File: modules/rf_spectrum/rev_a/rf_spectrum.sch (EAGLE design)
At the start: 43 parts, among them J1 MODULE_GENERIC, J7 TC2030-JLINK-L, P1 MOLEX_73251-135X, P2 MOLEX_73251-135X, P3 MOLEX_73251-135X, U1 SAM4LC8AA, U2 MWSUB3G, U3 SKY13317, U7 TLV62130, X1 16MHz

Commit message: schematic done, much routing done
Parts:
- removed C1, C2: 8pF, passives:CAPACITOR0603_CAP
- removed C16, C17, C18, C19: 100nF, passives:CAPACITOR0603_CAP
- removed C20: 100nF, passives:CAPACITOR0402_CAP
- removed C24: 4.7uF, passives:CAPACITOR0402_CAP
- removed FB1: 1.5kΩ, passives:FERRITE_BEAD0603
- removed L2: 22uH, signpost:LHQ3NP
- removed R15, R16: 100k, passives:RESISTOR0603_RES
- removed R25: 0, passives:RESISTOR0603_RES
- removed R7: 10k, passives:RESISTOR0603_RES
- removed TP11, TP12, TP13, TP14, TP15, TP16: TEST_POINT_0.040IN, headers:TEST_POINT_0.040IN
- removed X1: 16MHz, crystals:FH1600015
- added C11: 10nF, passives:CAPACITOR0402_CAP
- added C12: 1uF, passives:CAPACITOR0402_CAP
- added C13, C14: 4.3pF, passives:CAPACITOR0402_CAP
- added C7: 4.7uF, passives:CAPACITOR0402_CAP
- added C8, C9: 100nF, passives:CAPACITOR0402_CAP
- added D1: GREEN, leds:LED0603
- added D2: RED, leds:LED0603
- added R1, R3, R4: 10k, passives:RESISTOR0402_RES
- added R2: 100k, passives:RESISTOR0402_RES
- added X2: ABS05-32.768KHZ-9-T, crystals:ABS05-32.768KHZ-9-T
- C3, C4, C5, C6: device passives:CAPACITOR0603_CAP -> passives:CAPACITOR0402_CAP
- J1: value MODULE_GENERIC -> MODULE_GENERIC_DEBUGSMT; device signpost:MODULE_GENERIC -> signpost:MODULE_GENERIC_DEBUGSMT
- U1: value SAM4LC8AA -> STM32L432KC; device chips:SAM4LC8AA -> chips:STM32L432KC
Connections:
- removed net !CONTROLLER_RESET: J7.!RESET, S1.P$2, U1.!RESET
- removed net CONTROLLER_BUCK/LDO_N: R25.2, R7.1, U1.PA02
- removed net CONTROLLER_SWDCLK: J7.SWDCLK, R16.1, U1.TCK
- removed net CONTROLLER_SWDIO: J7.SWDIO, R15.1, U1.PA03
- removed net CONTROLLER_XIN: C1.1, U1.PA00, X1.2
- removed net CONTROLLER_XOUT: C2.1, U1.PA01, X1.1
- removed net N$32: C16.1, FB1.P$1, U1.VDDANA
- removed net N$44: C20.1, C24.1, L2.1, U1.VDDOUT
- removed net N$52: L2.2, U1.VDDCORE
- removed net N$53: U1.BIASH, U1.BIASL
- removed net N$54: U1.CAPH, U1.CAPL
- new net !RST: J1.DBG_!RESET, J7.!RESET, S1.P$2, U1.!RST
- new net DBG_GPIO1: J1.DBG_GPIO1, R3.2, U1.PB0
- new net DBG_GPIO2: J1.DBG_GPIO2, R4.2, U1.PB1
- new net DBG_RX: J1.DBG_RX, U1.PA3
- new net DBG_TX: J1.DBG_TX, U1.PA2
- new net N$10: C13.1, U1.PC15/OSC32OUT, X2.2
- new net N$11: R1.2, U1.PH3/BOOT0
- new net N$12: D1.ANODE, R3.1
- new net N$13: D2.ANODE, R4.1
- new net N$9: C14.1, U1.PC14/OSC32IN, X2.1
- new net SWDCLK: J1.DBG_SWDCLK, J7.SWDCLK, U1.PA14/SWCLK
- new net SWDIO: J1.DBG_SWDIO, J7.SWDIO, U1.PA13/SWDIO
- net 3V3: now also C11.1, C12.1, C7.1, C8.1, C9.1, R2.2, U1.VDD, U1.VDDA/VREF; no longer C17.1, C18.1, C19.1, FB1.P$2, R15.2, R16.2, R7.2, U1.VDDIN, U1.VDDIO, U1.VLCD, U1.VLCDIN
- net GND: now also C11.2, C12.2, C13.2, C14.2, C7.2, C8.2, C9.2, D1.CATHODE, D2.CATHODE, R1.1, U1.VSS; no longer C1.2, C16.2, C17.2, C18.2, C19.2, C2.2, C20.2, C24.2, R25.1, TP11.TESTPOINT, U1.GND, U1.GNDANA, X1.GND
- net MOD_IN: now also U1.PB5; no longer TP14.TESTPOINT, U1.PA20
- net MOD_OUT: now also U1.PB3/JTDO/SWO; no longer TP15.TESTPOINT, U1.PA19
- net PPS: now also U1.PA0/CLKIN; no longer TP16.TESTPOINT, U1.PA18
- net RF_ANT1: now also U1.PA4; no longer U1.PA09
- net RF_ANT2: now also U1.PA5; no longer U1.PA10
- net RF_ANT3: now also U1.PA6; no longer U1.PA11
- net RF_GPIO2: now also U1.PA15/JTDI; no longer U1.PA13
- net RF_GPIO3: now also R2.1, U1.PA1; no longer U1.PA06
- net RF_RESET: now also U1.PA8; no longer U1.PA14
- net RF_RX: now also U1.PB6; no longer U1.PA07
- net RF_TX: now also U1.PB7; no longer U1.PA05
- net SCL: now also U1.PA7, U1.PA9; no longer TP12.TESTPOINT, U1.PA24
- net SDA: now also U1.PA10, U1.PB4/!JTRST; no longer TP13.TESTPOINT, U1.PA23
- net USB+: now also U1.PA12; no longer U1.PA26
- net USB-: now also U1.PA11; no longer U1.PA25
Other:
- note added: "LFOSC can auto trim HFRC OSC to 0.25%"
- note removed: "Controller"

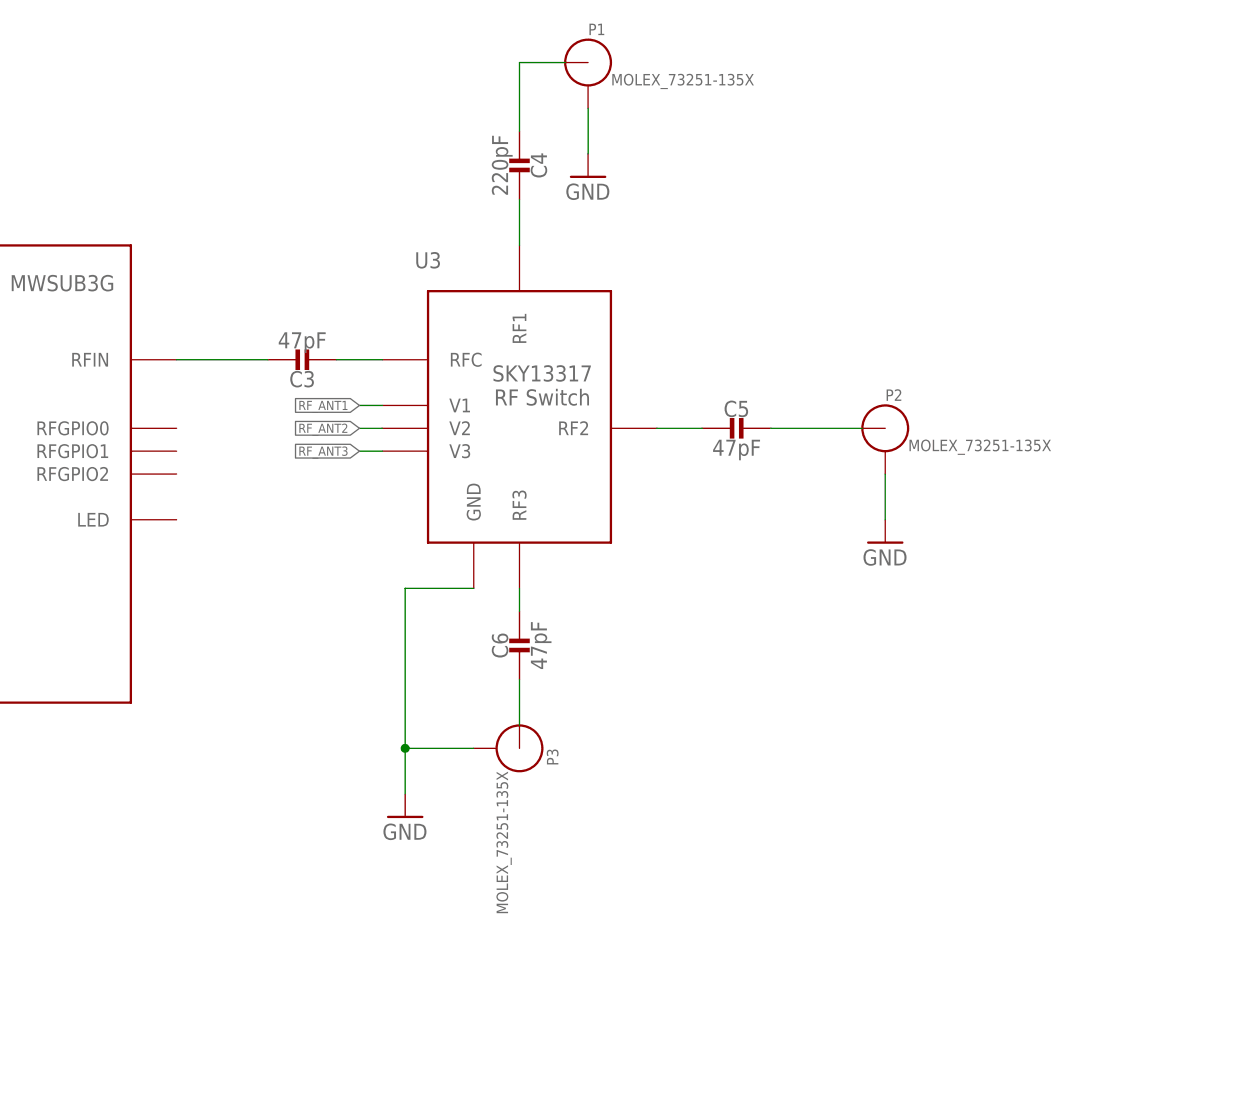
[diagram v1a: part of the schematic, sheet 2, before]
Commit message: finished routing, no silk yet
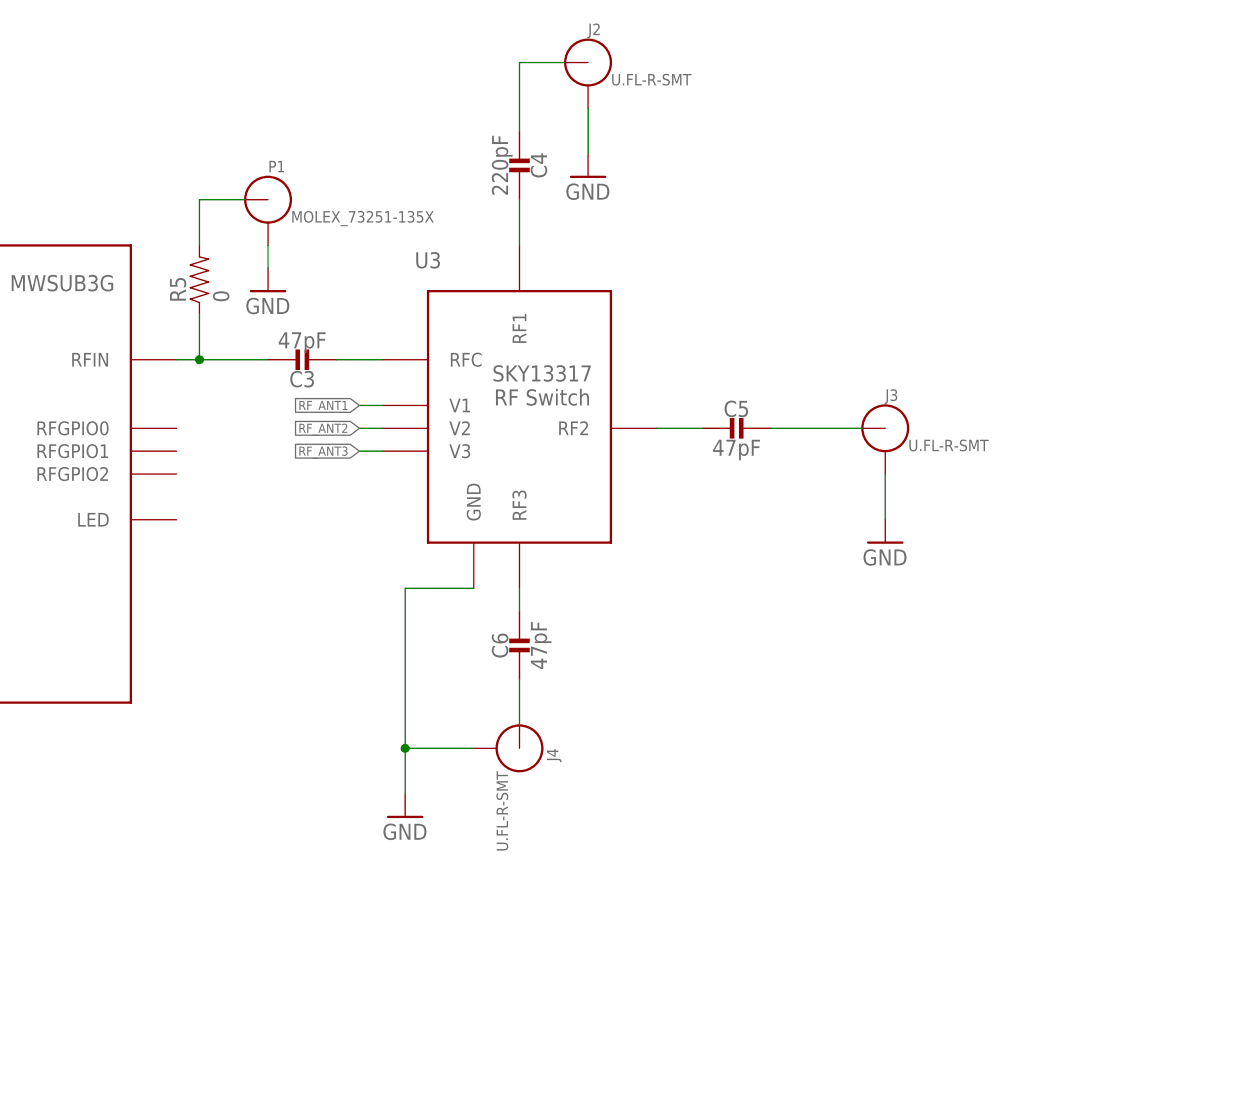
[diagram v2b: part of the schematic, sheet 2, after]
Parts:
- removed P2, P3: MOLEX_73251-135X, connector:MOLEX_73251-135X
- added J2, J3, J4: U.FL-R-SMT, connector:U.FL-R-SMT
- added R5: 0, passives:RESISTOR0402_RES
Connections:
- new net N$14: P1.ANT, R5.2
- net GND: now also J2.P$2, J3.P$2, J4.P$2; no longer P2.P$2, P3.P$2
- net N$1: now also R5.1
- net N$4: now also J2.ANT; no longer P1.ANT
- net N$6: now also J3.ANT; no longer P2.ANT
- net N$8: now also J4.ANT; no longer P3.ANT
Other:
- moved on the sheet: P1
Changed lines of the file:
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@@
 <part name="S1" library="switches" deviceset="B3U" device="-1000P"/>
 <part name="U2" library="signpost" deviceset="MWSUB3G" device=""/>
-<part name="P1" library="connector" deviceset="MOLEX_73251-135X" device=""/>
-<part name="P2" library="connector" deviceset="MOLEX_73251-135X" device=""/>
-<part name="P3" library="connector" deviceset="MOLEX_73251-135X" device=""/>
 <part name="GND1" library="umich" deviceset="GND" device=""/>
 <part name="U3" library="chips" deviceset="SKY13317" device=""/>
@@
 <part name="R4" library="passives" deviceset="RESISTOR" device="0402_RES" value="10k"/>
 <part name="GND9" library="umich" deviceset="GND" device=""/>
+<part name="J2" library="connector" deviceset="U.FL-R-SMT" device=""/>
+<part name="J3" library="connector" deviceset="U.FL-R-SMT" device=""/>
+<part name="J4" library="connector" deviceset="U.FL-R-SMT" device=""/>
+<part name="P1" library="connector" deviceset="MOLEX_73251-135X" device=""/>
+<part name="R5" library="passives" deviceset="RESISTOR" device="0402_RES" value="0"/>
+<part name="GND10" library="umich" deviceset="GND" device=""/>
 </parts>
 <sheets>
@@
 <instance part="FRAME2" gate="G$2" x="147.32" y="0"/>
 <instance part="U2" gate="G$1" x="106.68" y="119.38"/>
-<instance part="P1" gate="G$1" x="170.18" y="167.64"/>
-<instance part="P2" gate="G$1" x="203.2" y="127"/>
-<instance part="P3" gate="G$1" x="162.56" y="91.44" rot="R270"/>
 <instance part="GND1" gate="1" x="78.74" y="91.44"/>
 <instance part="U3" gate="G$1" x="157.48" y="116.84"/>
@@
 <instance part="GND4" gate="1" x="170.18" y="154.94"/>
 <instance part="R2" gate="G$1" x="60.96" y="124.46" rot="R90"/>
+<instance part="J2" gate="G$1" x="170.18" y="167.64"/>
+<instance part="J3" gate="G$1" x="203.2" y="127"/>
+<instance part="J4" gate="G$1" x="162.56" y="91.44" rot="R270"/>
+<instance part="P1" gate="G$1" x="134.62" y="152.4"/>
+<instance part="R5" gate="G$1" x="127" y="144.78" rot="R90"/>
+<instance part="GND10" gate="1" x="134.62" y="142.24"/>
 </instances>
 <busses>
@@
 <pinref part="U2" gate="G$1" pin="RFIN"/>
 <pinref part="C3" gate="G$1" pin="1"/>
-<wire x1="124.46" y1="134.62" x2="134.62" y2="134.62" width="0.1524" layer="91"/>
+<wire x1="124.46" y1="134.62" x2="127" y2="134.62" width="0.1524" layer="91"/>
+<pinref part="R5" gate="G$1" pin="1"/>
+<wire x1="127" y1="134.62" x2="134.62" y2="134.62" width="0.1524" layer="91"/>
+<wire x1="127" y1="139.7" x2="127" y2="134.62" width="0.1524" layer="91"/>
+<junction x="127" y="134.62"/>
 </segment>
 </net>
@@
 </segment>
 <segment>
-<pinref part="P1" gate="G$1" pin="P$2"/>
 <pinref part="GND4" gate="1" pin="GND"/>
 <wire x1="170.18" y1="162.56" x2="170.18" y2="157.48" width="0.1524" layer="91"/>
-</segment>
-<segment>
-<pinref part="P2" gate="G$1" pin="P$2"/>
+<pinref part="J2" gate="G$1" pin="P$2"/>
+</segment>
+<segment>
 <pinref part="GND3" gate="1" pin="GND"/>
 <wire x1="203.2" y1="121.92" x2="203.2" y2="116.84" width="0.1524" layer="91"/>
-</segment>
-<segment>
-<pinref part="P3" gate="G$1" pin="P$2"/>
+<pinref part="J3" gate="G$1" pin="P$2"/>
+</segment>
+<segment>
 <wire x1="157.48" y1="91.44" x2="149.86" y2="91.44" width="0.1524" layer="91"/>
 <pinref part="GND2" gate="1" pin="GND"/>
@@
 <wire x1="149.86" y1="109.22" x2="149.86" y2="91.44" width="0.1524" layer="91"/>
 <junction x="149.86" y="91.44"/>
+<pinref part="J4" gate="G$1" pin="P$2"/>
+</segment>
+<segment>
+<pinref part="GND10" gate="1" pin="GND"/>
+<pinref part="P1" gate="G$1" pin="P$2"/>
+<wire x1="134.62" y1="144.78" x2="134.62" y2="147.32" width="0.1524" layer="91"/>
 </segment>
 </net>
@@
 <pinref part="C4" gate="G$1" pin="2"/>
 <wire x1="162.56" y1="160.02" x2="162.56" y2="167.64" width="0.1524" layer="91"/>
-<pinref part="P1" gate="G$1" pin="ANT"/>
 <wire x1="162.56" y1="167.64" x2="167.64" y2="167.64" width="0.1524" layer="91"/>
+<pinref part="J2" gate="G$1" pin="ANT"/>
 </segment>
 </net>
@@
 <segment>
 <pinref part="C5" gate="G$1" pin="1"/>
-<pinref part="P2" gate="G$1" pin="ANT"/>
 <wire x1="190.5" y1="127" x2="200.66" y2="127" width="0.1524" layer="91"/>
+<pinref part="J3" gate="G$1" pin="ANT"/>
 </segment>
 </net>
@@
 <segment>
 <pinref part="C6" gate="G$1" pin="2"/>
-<pinref part="P3" gate="G$1" pin="ANT"/>
 <wire x1="162.56" y1="99.06" x2="162.56" y2="93.98" width="0.1524" layer="91"/>
+<pinref part="J4" gate="G$1" pin="ANT"/>
 </segment>
 </net>
@@
 </segment>
 </net>
+<net name="N$14" class="0">
+<segment>
+<pinref part="R5" gate="G$1" pin="2"/>
+<wire x1="127" y1="147.32" x2="127" y2="152.4" width="0.1524" layer="91"/>
+<pinref part="P1" gate="G$1" pin="ANT"/>
+<wire x1="127" y1="152.4" x2="132.08" y2="152.4" width="0.1524" layer="91"/>
+</segment>
+</net>
